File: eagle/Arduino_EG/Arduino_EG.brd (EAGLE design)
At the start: 94 x 71.1 mm, 24 parts, among them CN1 PWR, IC1 LM358, Q1 2N7000, T1 2SA1015

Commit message: Update eagle files
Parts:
- added JP9: TP-GND, pinhead:1X02
- C2, C4: value 22uF -> 47uF
- CN1: value PWR -> +9VPWR
- JP8: value SyncIn -> GateIn
- U$1: value ABK-PRO-MINI -> PRO-MINI; device Arduino-clone:ABK-PRO-MINI -> Arduino-clone:PRO-MINI
- moved U$1 17.8 mm to (31.8, 47.0)
- moved C4 2.54 mm to (15.2, 21.6)
- moved CN1 2.54 mm to (7.62, 21.6)
- moved JP1 2.54 mm to (68.6, 43.2)
- moved C1 1.80 mm to (72.4, 20.3), turned to 180 degrees
- turned C2 to 90 degrees
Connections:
- net D4: now also U$1.D5; no longer U$1.D4
- net D5: now also U$1.D6; no longer U$1.D5
- net D6: now also U$1.D7; no longer U$1.D6
- net GND: now also JP9.1, JP9.2
- net N$13: now also U$1.D3; no longer U$1.D2
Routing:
- net GND: track 0.00 -> 138.4 mm, vias 0 -> 2
- net A0: track 0.00 -> 42.7 mm
- net +5V: track 0.00 -> 30.5 mm, vias 0 -> 2
- net V+: track 0.00 -> 20.9 mm
- net D5: track 0.00 -> 15.2 mm, vias 0 -> 2
- net N$3: track 0.00 -> 15.2 mm
- net OUT: track 0.00 -> 12.7 mm
- net N$2: track 0.00 -> 11.2 mm
- net N$9: track 0.00 -> 5.08 mm
- net N$4: track 0.00 -> 5.08 mm
- net N$5: track 0.00 -> 5.08 mm
- net N$1: track 0.00 -> 5.08 mm
- net N$13: track 0.00 -> 2.54 mm
- net N$8: track 0.00 -> 2.54 mm
- net N$6: track 0.00 -> 2.54 mm
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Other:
- board text added: "Arduino EG"
- board text added: "http://dad8893.blogspot.com/"
- board text added: "はピンソケットで実装"

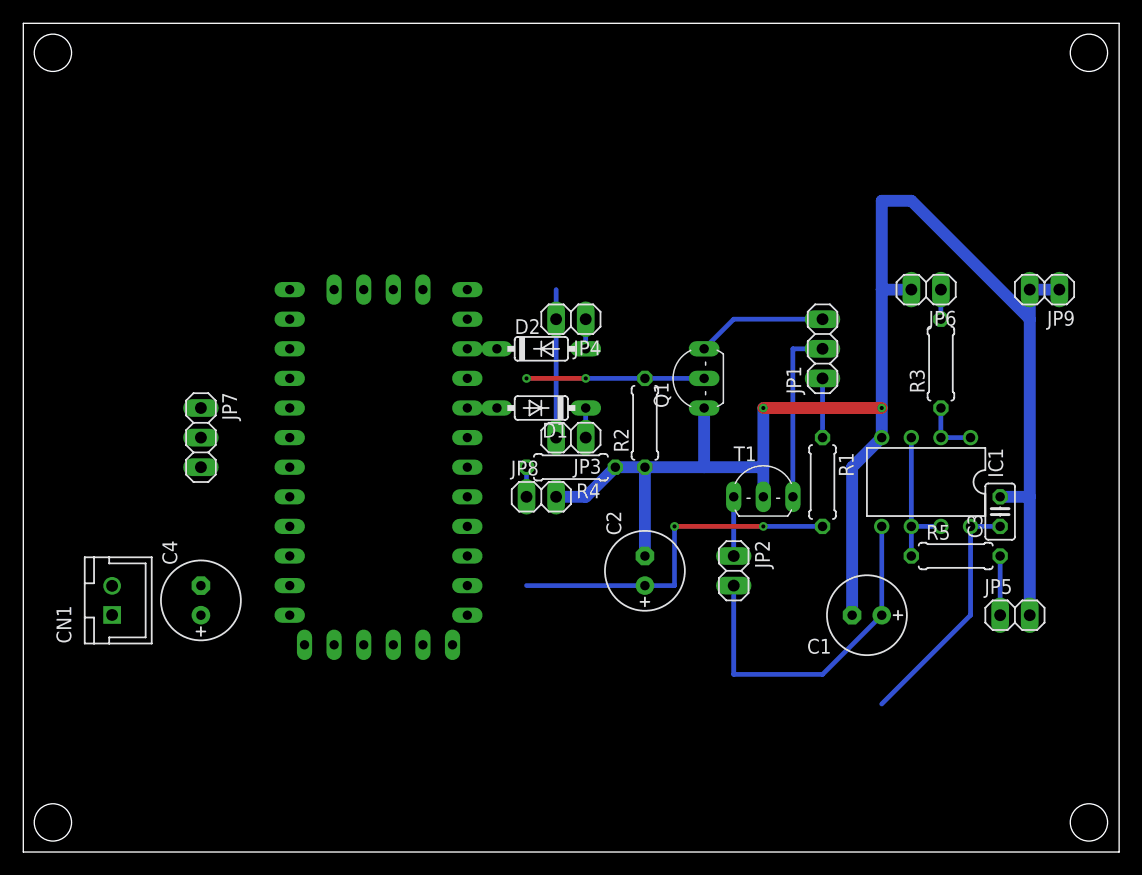
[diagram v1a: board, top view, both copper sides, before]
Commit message: Update Arduino sketch, Eagle files
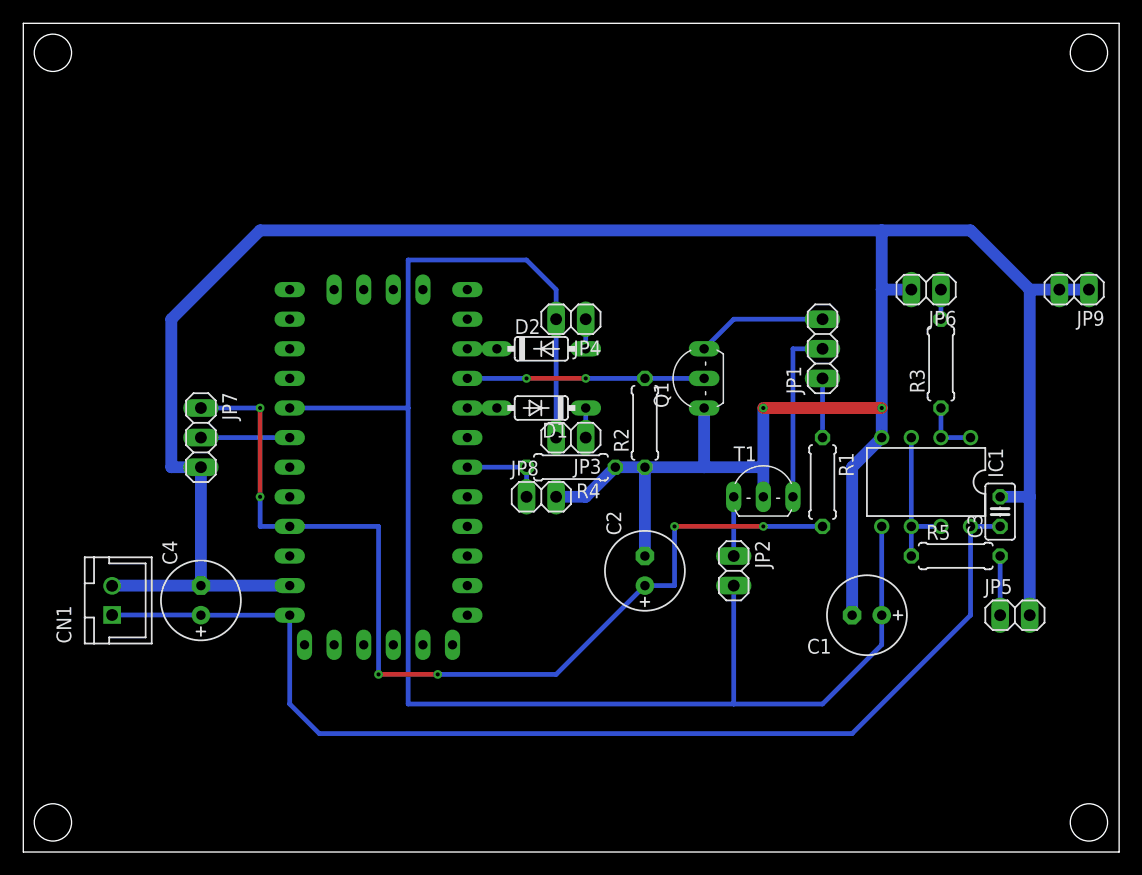
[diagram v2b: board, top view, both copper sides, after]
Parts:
- D1, D2: value 1N4148DO35-7 -> 1N4148
- moved JP9 2.54 mm to (90.2, 48.3)
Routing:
- net GND: track 138.4 -> 241.1 mm
- net A0: track 42.7 -> 137.8 mm
- net V+: track 20.9 -> 96.7 mm
- net +5V: track 30.5 -> 84.4 mm, vias 2 -> 6
- net N$10: track 0.00 -> 7.62 mm
- net N$13: track 2.54 -> 7.62 mm
- net D5: track 15.2 -> 20.3 mm
- net D6: track 0.00 -> 2.54 mm
- net D4: track 0.00 -> 2.54 mm

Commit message: Update eagle files
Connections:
- removed net D4: D1.A, U$1.D5
- new net D7: D2.C, U$1.D7
- net D5: now also D1.A, U$1.D5; no longer Q1.2, R2.2, U$1.D6
- net D6: now also Q1.2, R2.2, U$1.D6; no longer D2.C, U$1.D7
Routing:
- net D6: track 2.54 -> 20.3 mm, vias 0 -> 2
- net D5: track 20.3 -> 2.54 mm, vias 2 -> 0
- net D7: track 0.00 -> 2.54 mm
- net D4: track 2.54 -> 0.00 mm
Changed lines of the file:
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@@
 <attribute name="SPICEPREFIX" value="C" x="53.34" y="24.13" size="1.778" layer="27" rot="R90" display="off"/>
 </element>
-<element name="C3" library="rcl" library_urn="urn:adsk.eagle:library:334" package="C025-025X050" package3d_urn="urn:adsk.eagle:package:23629/2" value="0.1uF" x="83.82" y="29.21" rot="R90">
+<element name="C3" library="rcl" library_urn="urn:adsk.eagle:library:334" package="C025-025X050" package3d_urn="urn:adsk.eagle:package:23629/2" value="0.1uF" x="83.82" y="29.21" smashed="yes" rot="R90">
+<attribute name="NAME" x="87.376" y="29.464" size="1.27" layer="25" ratio="10" rot="R90"/>
 <attribute name="SPICEPREFIX" value="C" x="83.82" y="29.21" size="1.778" layer="27" rot="R90" display="off"/>
+<attribute name="VALUE" x="86.614" y="26.924" size="1.27" layer="27" ratio="10" rot="R90"/>
 </element>
 <element name="C4" library="rcl" library_urn="urn:adsk.eagle:library:334" package="E2,5-7" package3d_urn="urn:adsk.eagle:package:23345/1" value="47uF" x="15.24" y="21.59" rot="R90">
@@
 </element>
 <element name="D1" library="diode" library_urn="urn:adsk.eagle:library:210" package="DO35-7" package3d_urn="urn:adsk.eagle:package:43339/1" value="1N4148" x="44.45" y="38.1" smashed="yes" rot="R180">
-<attribute name="NAME" x="46.736" y="36.83" size="1.27" layer="25" ratio="10" rot="R180"/>
+<attribute name="NAME" x="44.196" y="40.64" size="1.27" layer="25" ratio="10" rot="R180"/>
 <attribute name="VALUE" x="44.196" y="40.767" size="1.27" layer="27" ratio="10" rot="R180"/>
 </element>
@@
 <element name="JP2" library="pinhead" library_urn="urn:adsk.eagle:library:325" package="1X02" package3d_urn="urn:adsk.eagle:package:22435/2" value="Rdcy" x="60.96" y="24.13" rot="R270"/>
 <element name="JP3" library="pinhead" library_urn="urn:adsk.eagle:library:325" package="1X02" package3d_urn="urn:adsk.eagle:package:22435/2" value="Ratk" x="46.99" y="35.56" smashed="yes" rot="R180">
-<attribute name="NAME" x="49.6062" y="33.7312" size="1.27" layer="25" ratio="10" rot="R180"/>
+<attribute name="NAME" x="44.5262" y="36.2712" size="1.27" layer="25" ratio="10" rot="R180"/>
 <attribute name="VALUE" x="44.45" y="36.195" size="1.27" layer="27" rot="R180"/>
 </element>
-<element name="JP4" library="pinhead" library_urn="urn:adsk.eagle:library:325" package="1X02" package3d_urn="urn:adsk.eagle:package:22435/2" value="Rrls" x="46.99" y="45.72" rot="R180"/>
+<element name="JP4" library="pinhead" library_urn="urn:adsk.eagle:library:325" package="1X02" package3d_urn="urn:adsk.eagle:package:22435/2" value="Rrls" x="46.99" y="45.72" smashed="yes" rot="R180">
+<attribute name="NAME" x="49.6062" y="48.9712" size="1.27" layer="25" ratio="10" rot="R180"/>
+<attribute name="VALUE" x="49.53" y="48.895" size="1.27" layer="27" rot="R180"/>
+</element>
 <element name="JP5" library="pinhead" library_urn="urn:adsk.eagle:library:325" package="1X02" package3d_urn="urn:adsk.eagle:package:22435/2" value="Out" x="85.09" y="20.32"/>
-<element name="JP6" library="pinhead" library_urn="urn:adsk.eagle:library:325" package="1X02" package3d_urn="urn:adsk.eagle:package:22435/2" value="INDICATOR" x="77.47" y="48.26" rot="R180"/>
+<element name="JP6" library="pinhead" library_urn="urn:adsk.eagle:library:325" package="1X02" package3d_urn="urn:adsk.eagle:package:22435/2" value="INDICATOR" x="77.47" y="48.26" smashed="yes" rot="R180">
+<attribute name="NAME" x="80.0862" y="51.5112" size="1.27" layer="25" ratio="10" rot="R180"/>
+<attribute name="VALUE" x="80.01" y="51.435" size="1.27" layer="27" rot="R180"/>
+</element>
 <element name="JP7" library="pinhead" library_urn="urn:adsk.eagle:library:325" package="1X03" package3d_urn="urn:adsk.eagle:package:22458/2" value="Rlvl" x="15.24" y="35.56" rot="R270"/>
-<element name="JP8" library="pinhead" library_urn="urn:adsk.eagle:library:325" package="1X02" package3d_urn="urn:adsk.eagle:package:22435/2" value="GateIn" x="44.45" y="30.48"/>
+<element name="JP8" library="pinhead" library_urn="urn:adsk.eagle:library:325" package="1X02" package3d_urn="urn:adsk.eagle:package:22435/2" value="GateIn" x="44.45" y="30.48" smashed="yes">
+<attribute name="NAME" x="41.8338" y="27.2288" size="1.27" layer="25" ratio="10"/>
+<attribute name="VALUE" x="41.91" y="27.305" size="1.27" layer="27"/>
+</element>
 <element name="R1" library="rcl" library_urn="urn:adsk.eagle:library:334" package="0207/7" package3d_urn="urn:adsk.eagle:package:23493/1" value="6.8k" x="68.58" y="31.75" rot="R270">
 <attribute name="SPICEPREFIX" value="R" x="68.58" y="31.75" size="1.778" layer="27" rot="R270" display="off"/>
@@
 </element>
 <element name="T1" library="transistor-neu-to92" library_urn="urn:adsk.eagle:library:397" package="TO92-ECB" package3d_urn="urn:adsk.eagle:package:28756/2" value="2SA1015" x="63.5" y="30.48"/>
-<element name="Q1" library="mylib2" package="TO92-" value="2N7000" x="58.42" y="40.64" rot="R90"/>
-<element name="R5" library="rcl" library_urn="urn:adsk.eagle:library:334" package="0207/7" package3d_urn="urn:adsk.eagle:package:23493/1" value="100" x="80.01" y="25.4">
+<element name="Q1" library="mylib2" package="TO92-" value="2N7000" x="58.42" y="40.64" smashed="yes" rot="R90">
+<attribute name="NAME" x="56.642" y="43.18" size="1.27" layer="25" ratio="10" rot="R90"/>
+<attribute name="VALUE" x="61.722" y="38.1" size="1.27" layer="27" ratio="10" rot="R90"/>
+</element>
+<element name="R5" library="rcl" library_urn="urn:adsk.eagle:library:334" package="0207/7" package3d_urn="urn:adsk.eagle:package:23493/1" value="100" x="80.01" y="25.4" smashed="yes">
+<attribute name="NAME" x="77.47" y="22.987" size="1.27" layer="25" ratio="10"/>
 <attribute name="SPICEPREFIX" value="R" x="80.01" y="25.4" size="1.778" layer="27" display="off"/>
+<attribute name="VALUE" x="77.724" y="24.8412" size="1.27" layer="27" ratio="10"/>
 </element>
 <element name="JP9" library="pinhead" library_urn="urn:adsk.eagle:library:325" package="1X02" package3d_urn="urn:adsk.eagle:package:22435/2" value="TP-GND" x="90.17" y="48.26" rot="R180"/>
@@
 <wire x1="48.26" y1="45.72" x2="48.26" y2="43.18" width="0.4064" layer="16"/>
 </signal>
-<signal name="D4">
+<signal name="D5">
 <contactref element="D1" pad="A"/>
 <contactref element="U$1" pad="D5"/>
 <wire x1="38.1" y1="38.1" x2="40.64" y2="38.1" width="0.4064" layer="16"/>
 </signal>
-<signal name="D5">
+<signal name="D6">
 <contactref element="R2" pad="2"/>
 <contactref element="Q1" pad="2"/>
@@
 <wire x1="38.1" y1="40.64" x2="43.18" y2="40.64" width="0.4064" layer="16"/>
 </signal>
-<signal name="D6">
+<signal name="D7">
 <contactref element="D2" pad="C"/>
 <contactref element="U$1" pad="D7"/>
